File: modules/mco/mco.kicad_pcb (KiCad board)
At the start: 2 copper layers, 30.5 x 68.6 mm, 22 parts, among them U1 ATtiny1616-M, U3 MCP6002-xSN

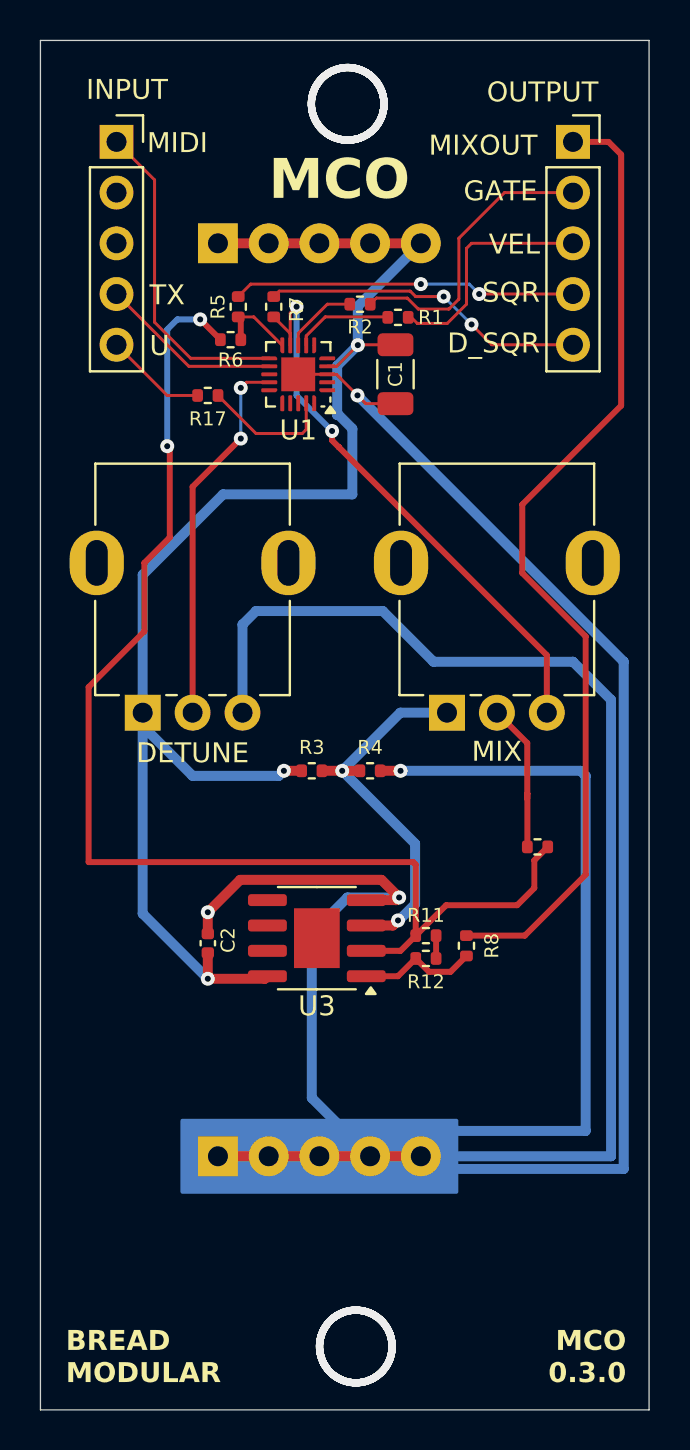
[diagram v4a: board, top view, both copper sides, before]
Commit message: Change uc to SOIC
Changing the packaging of the micro to SOIC for easier hand soldering.
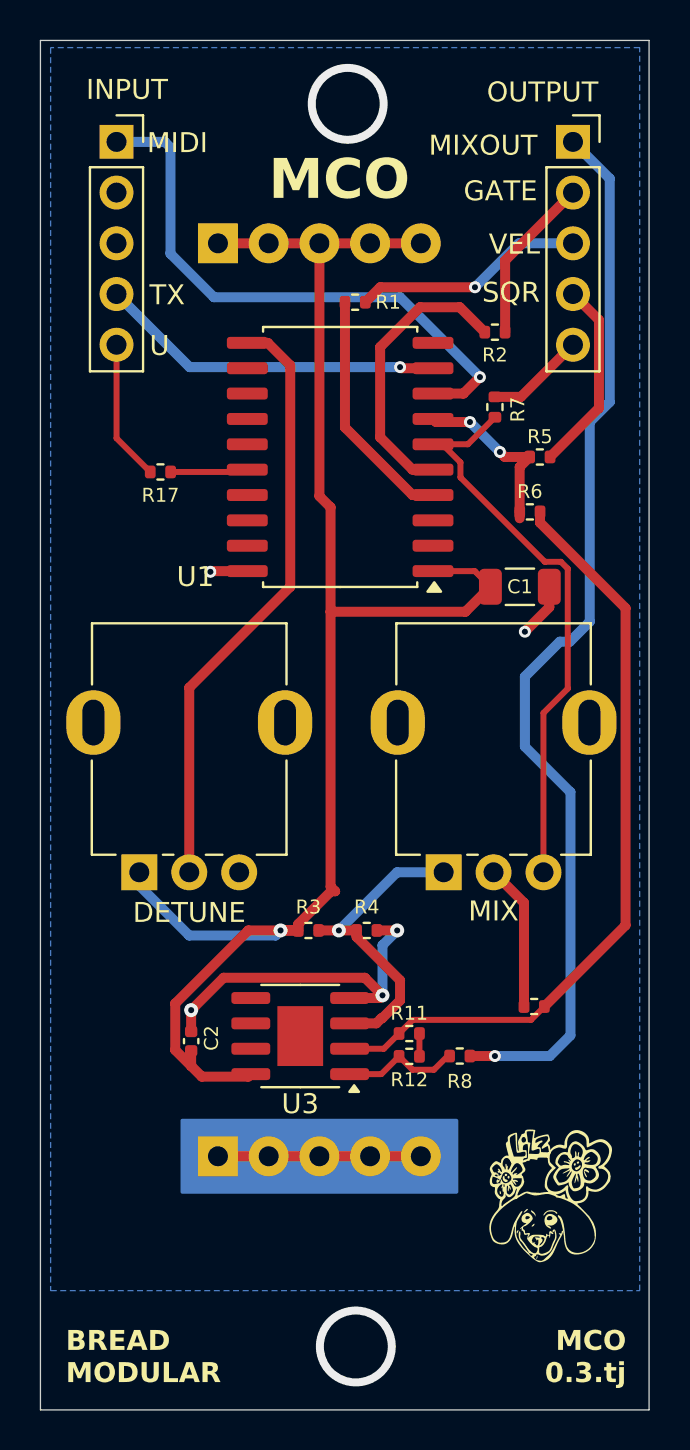
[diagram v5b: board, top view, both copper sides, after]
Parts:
- U1: value ATtiny1616-M -> ATtiny1616-S; footprint Package_DFN_QFN:VQFN-20-1EP_3x3mm_P0.4mm_EP1.7x1.7mm -> Package_SO:SOIC-20W_7.5x12.8mm_P1.27mm
- moved R6 17.3 mm to (71.5, 64.2), turned to 0 degrees
- moved R5 16.9 mm to (72.0, 61.5), turned to 0 degrees
- moved C1 12.3 mm to (71.0, 68.0), turned to 180 degrees
- moved R7 12.2 mm to (69.8, 59.0)
- moved R10 8.00 mm to (71.7, 89.0)
- moved R3 8.00 mm to (60.4, 85.2)
- moved R4 8.00 mm to (63.3, 85.2)
- moved RV1 8.00 mm to (51.9, 82.3)
- moved RV2 8.00 mm to (67.2, 82.3)
- moved R2 6.90 mm to (69.8, 55.2)
- moved R8 5.53 mm to (68.0, 91.5), turned to 0 degrees
- moved C2 4.97 mm to (54.5, 90.8)
- moved R11 4.97 mm to (65.5, 90.4)
- moved R12 4.97 mm to (65.5, 91.5)
- moved U3 4.97 mm to (60.0, 90.5)
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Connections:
- U1 pad 1: unconnected-(U1-PA2-Pad1) -> V_SUPPLY
- U1 pad 10: FUNDAMENTAL_TONE -> unconnected-(U1-PB1-Pad10)
- U1 pad 11: MIDI -> V_DETUNED
- U1 pad 12: TX -> unconnected-(U1-PC0-Pad12)
- U1 pad 14: V_DETUNED -> unconnected-(U1-PC2-Pad14)
- U1 pad 16: unconnected-(U1-PC1-Pad16) -> Net-(U1-~{RESET}/PA0)
- U1 pad 19: Net-(U1-~{RESET}/PA0) -> unconnected-(U1-PA3-Pad19)
- U1 pad 20: unconnected-(U1-PA1-Pad20) -> GND
- U1 pad 3: GND -> unconnected-(U1-PA5-Pad3)
- U1 pad 4: V_SUPPLY -> Net-(U1-PA6)
- U1 pad 5: unconnected-(U1-PA4-Pad5) -> Net-(U1-PA7)
- U1 pad 6: unconnected-(U1-PA5-Pad6) -> DETUNED_TONE
- U1 pad 7: Net-(U1-PA6) -> FUNDAMENTAL_TONE
- U1 pad 8: Net-(U1-PA7) -> MIDI
- U1 pad 9: DETUNED_TONE -> TX
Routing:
- net GND: track 196.0 -> 34.1 mm, vias 4 -> 5
- net Net-(U3A--): track 63.9 -> 39.0 mm, vias 2 -> 0
- net MIDI: track 16.3 -> 28.9 mm, vias 0 -> 1
- net V_DETUNED: track 18.8 -> 30.1 mm, vias 2 -> 0
- net DETUNED_OUT: track 16.2 -> 4.99 mm, vias 2 -> 0
- net Net-(U1-PA7): track 3.79 -> 14.4 mm
- net TX: track 9.15 -> 17.4 mm, vias 0 -> 1
- net SQUARE_OUT: track 17.2 -> 9.71 mm, vias 2 -> 0
- net Net-(U1-PA6): track 5.01 -> 12.1 mm
- net GATE: track 14.7 -> 8.40 mm
- net V_SUPPLY: track 76.6 -> 82.5 mm, vias 3 -> 1
- net FUNDAMENTAL_TONE: track 3.99 -> 8.91 mm, vias 0 -> 2
- net MIX_OUT: track 49.3 -> 54.0 mm, vias 0 -> 1
- net V_MID: track 19.4 -> 15.8 mm, vias 2 -> 1
- net Net-(U1-~{RESET}/PA0): track 6.61 -> 3.89 mm
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- added copper zone on B.Cu, net GND
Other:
- board text added: "MCO 0.3.tj"
- board text removed: "D_SQR"
- board text removed: "MCO 0.3.0"
